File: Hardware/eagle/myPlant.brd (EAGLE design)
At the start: 152.4 x 25.4 mm, 37 parts, among them U1 SI7021, U2 ALS-PT19, U3 FSA3357, U4 TPS22860, U5 NCP1402, X1 ESP-12

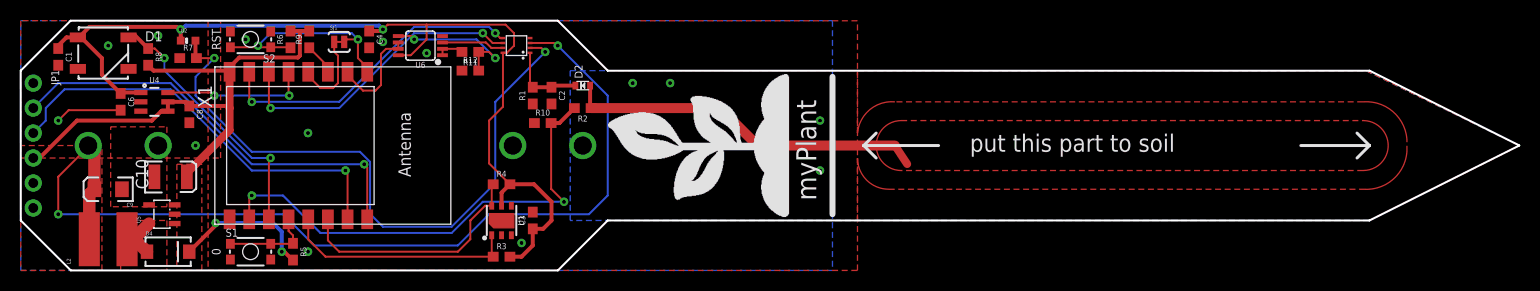
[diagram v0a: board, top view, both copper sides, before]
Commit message: Corrected DRC errors
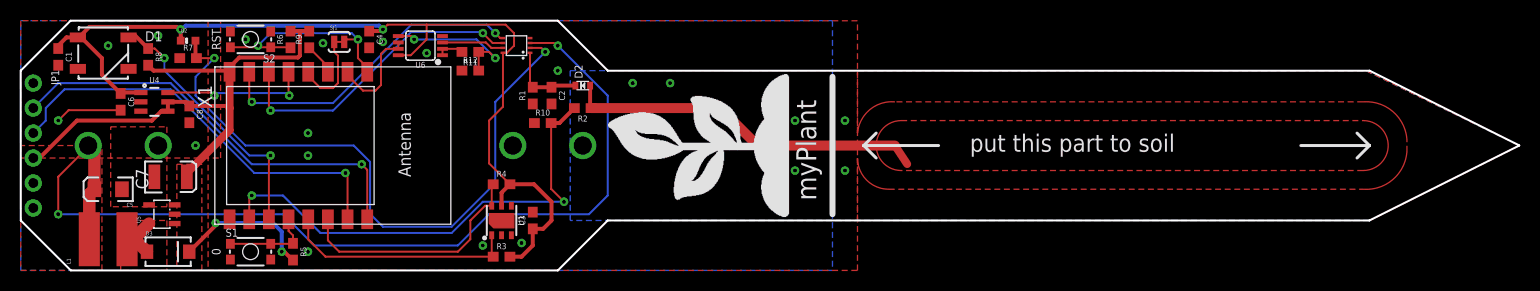
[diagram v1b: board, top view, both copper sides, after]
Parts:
- added LOGO2: OSHW-LOGOS, SparkFun-Aesthetics:OSHW-LOGO-S
- U6: value (none) -> LMV358
- moved FRAME1 7.62 mm to (20.8, -9.14)
- renumbered C10 to C7, C9 to C5, D4 to D3, L2 to L1
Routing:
- net GND: vias 18 -> 20
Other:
- board text added: "Alexandre Houde"
